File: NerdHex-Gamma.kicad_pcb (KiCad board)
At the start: 6 copper layers, 110 x 200 mm, 340 parts, among them J1 Connector 02x01, J8 Conn_01x06, M1 Fan_4pin, M2 Fan_4pin, U1 AP3211, U10 EMC2302-1, U11 TXU0102-DCU, U12 TMP1075, U13 TMP1075, U14 TXU0304PW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

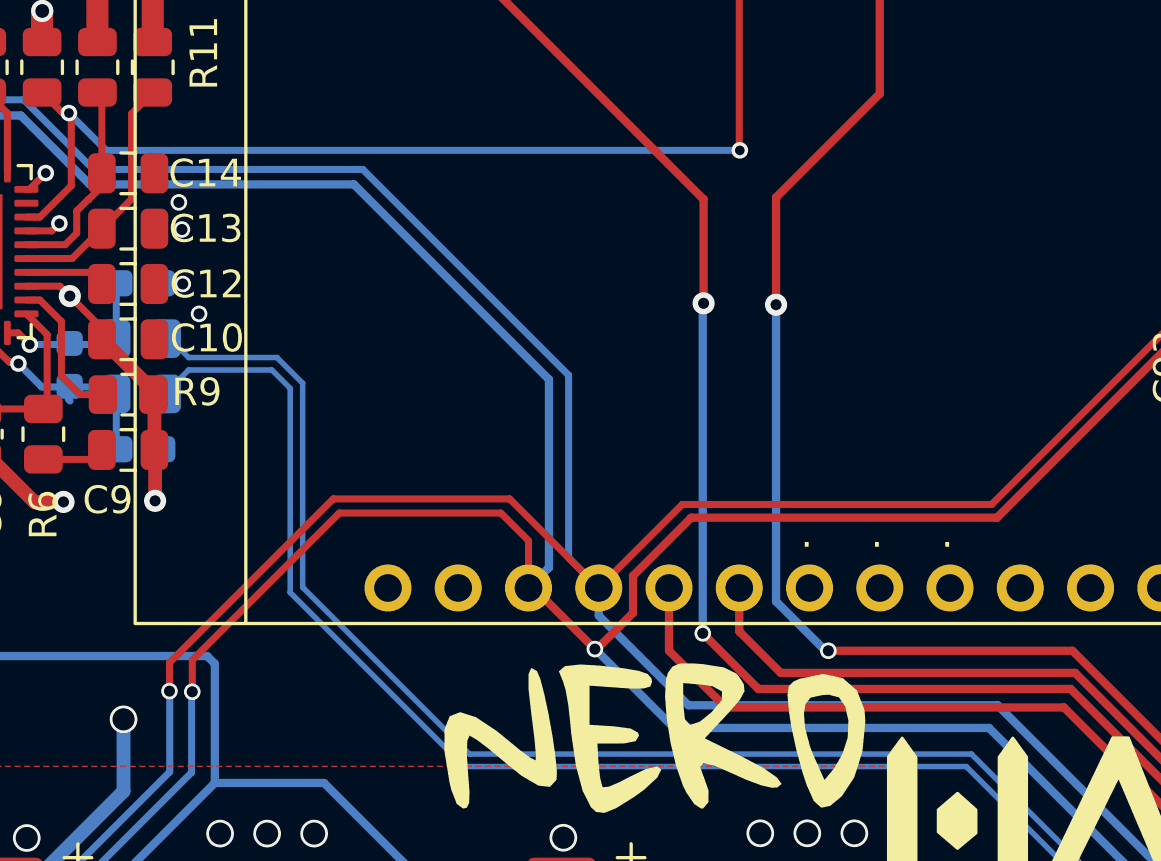
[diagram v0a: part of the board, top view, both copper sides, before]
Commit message: 12V Input + i2c pullups
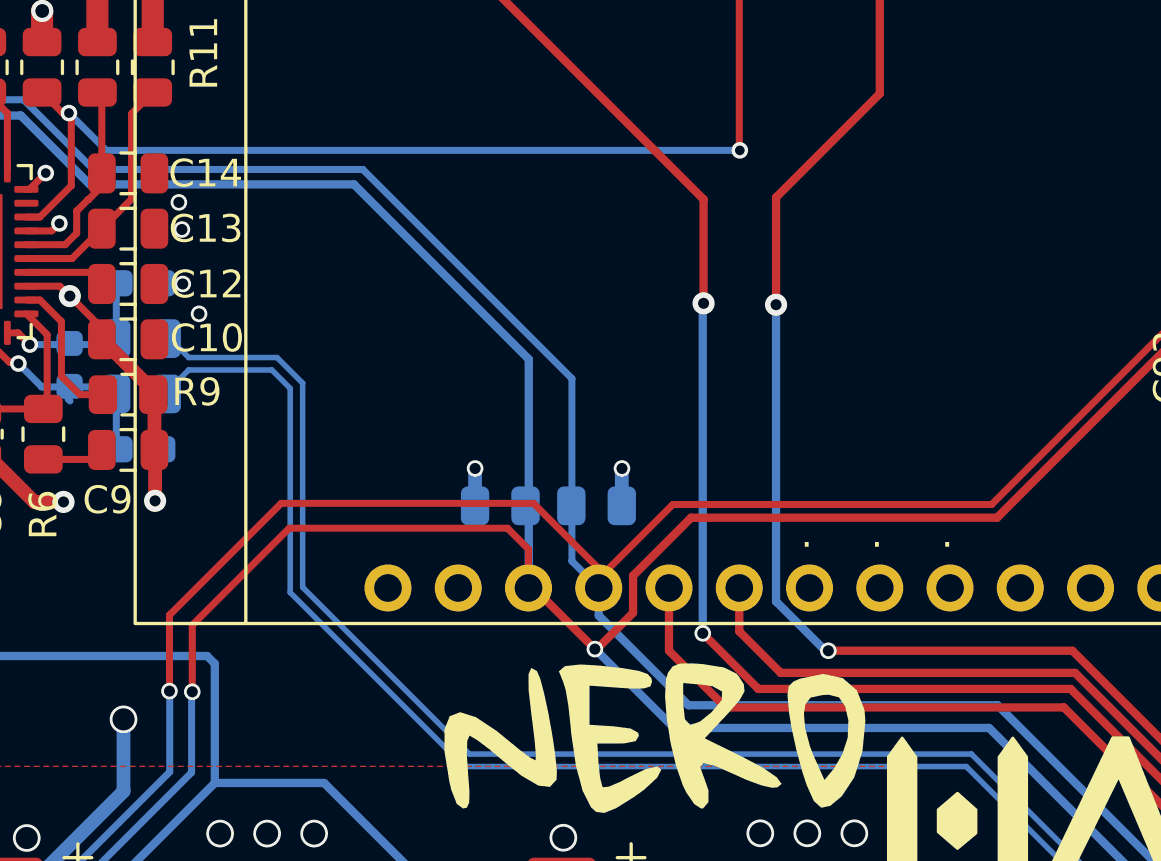
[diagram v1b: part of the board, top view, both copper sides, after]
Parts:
- added R32: 2.7k, Resistor_SMD:R_0805_2012Metric, B.Cu at (90.7, 56.5)
- added R35: 2.7k, Resistor_SMD:R_0805_2012Metric, B.Cu at (94.2, 56.5)
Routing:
- net +3V3: track 144.2 -> 146.9 mm, vias 12 -> 14
- net /T-Display-S3/SDA: track 261.7 -> 263.2 mm
- net /T-Display-S3/SCL: track 259.1 -> 258.6 mm
